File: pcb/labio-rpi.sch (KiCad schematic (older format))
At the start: 12 parts, among them IC201 AT24CS32-XHM, P1 CONN_02X20, U201 AP7365_SOT-23-5

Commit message: add cmu + wise logos, clean up silk, review for final errors
* move audio jack in so copper pads are inside board
* add logos/identifier text on silk and copper
* change rpi connector for no paste (to be left depopulated at fab)
* change soldermask expansion to 2 mils/3 mils minimum width
* add labels for motor, ADC, codec headers
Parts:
- P1: footprint labio-special:Pin_Header_Straight_TH-SMT_2x20 -> labio-special:Pin_Header_Straight_TH-SMT-NoPaste_2x20
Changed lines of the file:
@@
 LIBS:valves
 LIBS:labio-special
+LIBS:wise_logo
+LIBS:cmu_logo
 LIBS:labio-cache
 EELAYER 25 0
@@
 F 0 "P1" H 4250 3100 50  0000 C CNN
 F 1 "CONN_02X20" V 4250 2050 50  0000 C CNN
-F 2 "labio-special:Pin_Header_Straight_TH-SMT_2x20" H 4250 1100 50  0001 C CNN
+F 2 "labio-special:Pin_Header_Straight_TH-SMT-NoPaste_2x20" H 4250 1100 50  0001 C CNN
 F 3 "" H 4250 1100 50  0000 C CNN
 	1    4250 2050

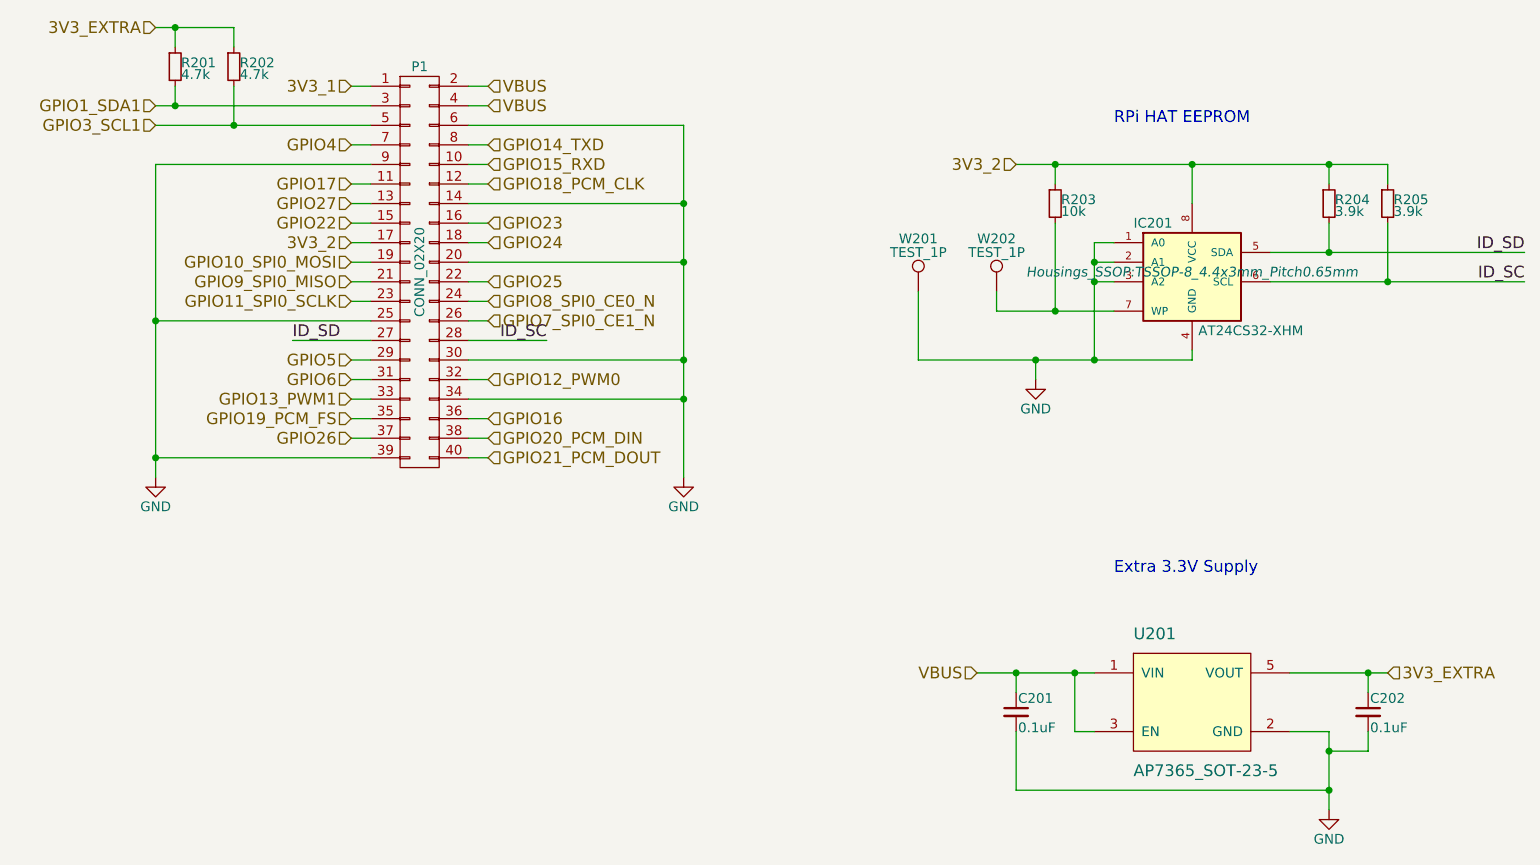
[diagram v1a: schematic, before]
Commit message: Fix board/bom errors from initial build
* Accelerometer (U501) footprint mirrored. Redraw footprint and adjust routing.
* Gyro (U505) footprint mirrored. Redraw footprint and adjust routing.
* Codec (U702) labed as wrong chip. Says WM8731 but should be 8750. Also fix in BOM.
* Should include OLED screen in BOM (not just the connector).
* Codec to TRRS caps have incorrect value. Says 220uF but should be 220pF.
* Mark RPi Hat EEPROM circuit as depopulated in schematic.
* Remove dangling trace near encoder headers.
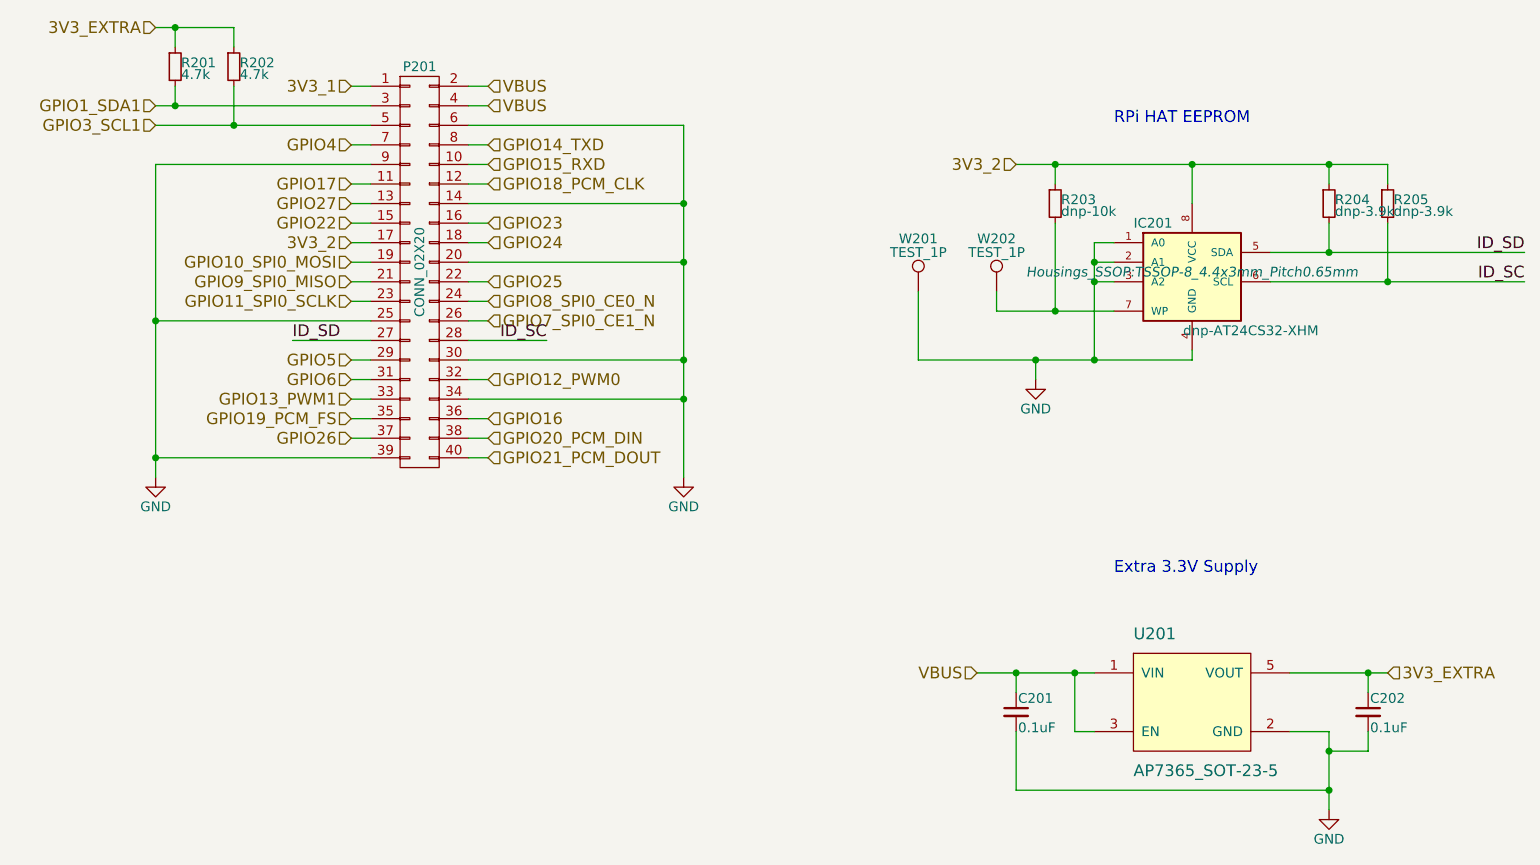
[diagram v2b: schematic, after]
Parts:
- IC201: value AT24CS32-XHM -> dnp-AT24CS32-XHM
- R203: value 10k -> dnp-10k
- R204, R205: value 3.9k -> dnp-3.9k
- renumbered P1 to P201
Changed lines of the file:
@@
 $EndDescr
 $Comp
-L CONN_02X20 P1
+L CONN_02X20 P201
 U 1 1 57269431
 P 4250 2050
-F 0 "P1" H 4250 3100 50  0000 C CNN
+F 0 "P201" H 4250 3100 50  0000 C CNN
 F 1 "CONN_02X20" V 4250 2050 50  0000 C CNN
 F 2 "labio-special:Pin_Header_Straight_TH-SMT-NoPaste_2x20" H 4250 1100 50  0001 C CNN
@@
 	3900 2900 4000 2900
 $Comp
-L GND #PWR01
+L GND #PWR201
 U 1 1 57477DAC
 P 2900 3100
-F 0 "#PWR01" H 2900 2850 50  0001 C CNN
+F 0 "#PWR201" H 2900 2850 50  0001 C CNN
 F 1 "GND" H 2900 2950 50  0000 C CNN
 F 2 "" H 2900 3100 50  0000 C CNN
@@
 GPIO21_PCM_DOUT
 $Comp
-L GND #PWR02
+L GND #PWR202
 U 1 1 5747813A
 P 5600 3100
-F 0 "#PWR02" H 5600 2850 50  0001 C CNN
+F 0 "#PWR202" H 5600 2850 50  0001 C CNN
 F 1 "GND" H 5600 2950 50  0000 C CNN
 F 2 "" H 5600 3100 50  0000 C CNN
@@
 P 8200 2050
 F 0 "IC201" H 8000 2300 50  0000 C CNN
-F 1 "AT24CS32-XHM" H 8500 1750 50  0000 C CNN
+F 1 "dnp-AT24CS32-XHM" H 8500 1750 50  0000 C CNN
 F 2 "Housings_SSOP:TSSOP-8_4.4x3mm_Pitch0.65mm" H 8200 2050 50  0000 C CIN
 F 3 "" H 8200 2050 50  0000 C CNN
@@
 P 7500 1700
 F 0 "R203" H 7530 1720 50  0000 L CNN
-F 1 "10k" H 7530 1660 50  0000 L CNN
+F 1 "dnp-10k" H 7530 1660 50  0000 L CNN
 F 2 "Resistors_SMD:R_0603" H 7500 1700 50  0001 C CNN
 F 3 "" H 7500 1700 50  0000 C CNN
@@
 P 8900 1700
 F 0 "R204" H 8930 1720 50  0000 L CNN
-F 1 "3.9k" H 8930 1660 50  0000 L CNN
+F 1 "dnp-3.9k" H 8930 1660 50  0000 L CNN
 F 2 "Resistors_SMD:R_0603" H 8900 1700 50  0001 C CNN
 F 3 "" H 8900 1700 50  0000 C CNN
@@
 P 9200 1700
 F 0 "R205" H 9230 1720 50  0000 L CNN
-F 1 "3.9k" H 9230 1660 50  0000 L CNN
+F 1 "dnp-3.9k" H 9230 1660 50  0000 L CNN
 F 2 "Resistors_SMD:R_0603" H 9200 1700 50  0001 C CNN
 F 3 "" H 9200 1700 50  0000 C CNN
@@
 $EndComp
 $Comp
-L GND #PWR03
+L GND #PWR203
 U 1 1 574789A2
 P 7400 2600
-F 0 "#PWR03" H 7400 2350 50  0001 C CNN
+F 0 "#PWR203" H 7400 2350 50  0001 C CNN
 F 1 "GND" H 7400 2450 50  0000 C CNN
 F 2 "" H 7400 2600 50  0000 C CNN
@@
 $EndComp
 $Comp
-L GND #PWR04
+L GND #PWR204
 U 1 1 5767CF14
 P 8900 4800
-F 0 "#PWR04" H 8900 4550 50  0001 C CNN
+F 0 "#PWR204" H 8900 4550 50  0001 C CNN
 F 1 "GND" H 8900 4650 50  0000 C CNN
 F 2 "" H 8900 4800 50  0000 C CNN

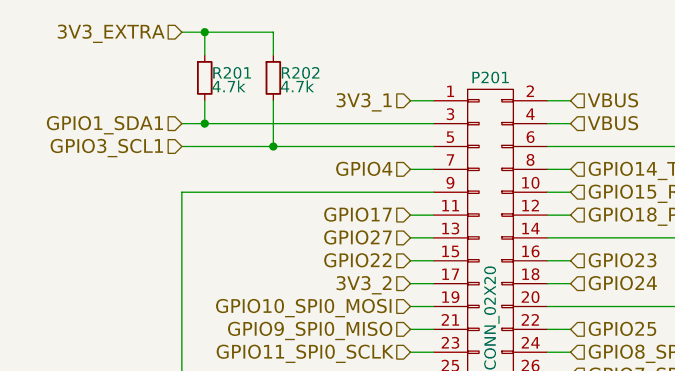
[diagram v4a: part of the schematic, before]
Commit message: Fix i2c addresses, pressure sensor footprint, consolidate BOM
* Schematic should list I2C addresses for accelerometer, gyro.
* Pressure sensor footprint (U502) has pins in the wrong order. Redraw footprint and adjust routing.
* Bump i2c and photodiode pullups to 2.2k
* Remove R505 near gyro
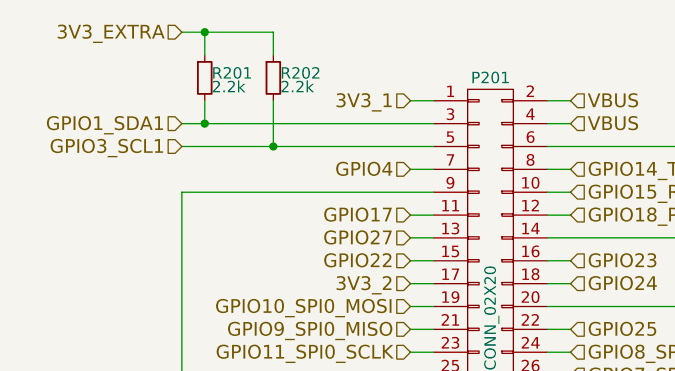
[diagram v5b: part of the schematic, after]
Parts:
- R201, R202: value 4.7k -> 2.2k
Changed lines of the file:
@@
 P 3300 1000
 F 0 "R202" H 3330 1020 50  0000 L CNN
-F 1 "4.7k" H 3330 960 50  0000 L CNN
+F 1 "2.2k" H 3330 960 50  0000 L CNN
 F 2 "Resistors_SMD:R_0603" H 3300 1000 50  0001 C CNN
 F 3 "" H 3300 1000 50  0000 C CNN
@@
 P 3000 1000
 F 0 "R201" H 3030 1020 50  0000 L CNN
-F 1 "4.7k" H 3030 960 50  0000 L CNN
+F 1 "2.2k" H 3030 960 50  0000 L CNN
 F 2 "Resistors_SMD:R_0603" H 3000 1000 50  0001 C CNN
 F 3 "" H 3000 1000 50  0000 C CNN
